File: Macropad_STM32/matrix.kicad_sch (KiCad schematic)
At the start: 85 parts, among them J10 Encoders + LED, J7 Power Connector, J9 Matrix, K1 Kailh Hotswap Socket, K10 Kailh Hotswap Socket, K11 Kailh Hotswap Socket, K12 Kailh Hotswap Socket, K13 Kailh Hotswap Socket, K14 Kailh Hotswap Socket, K15 Kailh Hotswap Socket, K16 Kailh Hotswap Socket, K2 Kailh Hotswap Socket, K3 Kailh Hotswap Socket, K4 Kailh Hotswap Socket, K5 Kailh Hotswap Socket, K6 Kailh Hotswap Socket, K7 Kailh Hotswap Socket, K8 Kailh Hotswap Socket, K9 Kailh Hotswap Socket, SW2 EC11 Encoder, SW3 EC11 Encoder

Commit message: Schematic changes Motherboard nearing completion
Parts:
- removed J10: Encoders + LED, Connector_JST:JST_EH_B7B-EH-A_1x07_P2.50mm_Vertical, symbol Connector_Generic:Conn_01x07
- removed J9: Matrix, Connector_JST:JST_EH_B8B-EH-A_1x08_P2.50mm_Vertical, symbol Connector_Generic:Conn_01x08
- C39, C40, C41, C42: now not fitted
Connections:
- net COL0: no longer K13.1, K14.1, K15.1, K16.1
- net COL1: no longer K10.1, K11.1, K12.1, K9.1
- new net COL2: K10.1, K11.1, K12.1, K9.1
- new net COL3: K13.1, K14.1, K15.1, K16.1
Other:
- company: (none) -> Irfaan
- title: (none) -> STM32 Macropad

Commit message: Revision 1 nearly finished
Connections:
- net ENC1_B is gone; now on net ENC1_A: C39.1, R31.2
- net ENC2_B is gone; now on net ENC2_A: C40.1, R35.2
- net VBUS is gone; now on net +5V: C20.1, C21.1, C29.1, C30.1, C31.1, C32.1, C33.1, C34.1, C35.1, C35.1, C36.1, C36.1, C37.1, C37.1, C38.1, C38.1, D29.1 (VDD), D30.1 (VDD), D31.1 (VDD), D32.1 (VDD), D33.1 (VDD), D34.1 (VDD), D35.1 (VDD), D36.1 (VDD), D37.1 (VDD), D38.1 (VDD), D39.1 (VDD), D40.1 (VDD), D41.1 (VDD), D42.1 (VDD), D43.1 (VDD), D44.1 (VDD), J7.1 (Pin_1)
- net +3.3V renamed +3V3
- net GND renamed GND1
- net GND1: no longer C20.2, C21.2, C29.2, C30.2
- net Key_LED renamed +5V
- new net: C20.2, C21.2, C29.2, C30.2
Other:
- moved on the sheet: C29, C31, C32, C33, C34, C35, C36, C37, C38, C39, C40, C41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

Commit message: Nearly finished Todo: - Fix silkscreen - Final check
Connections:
- net +5V: no longer R27.1
- net ENC1_A: no longer C39.1, R31.2
- net ENC2_A: no longer C40.1, R35.2
- net GND1: now also C20.2, C21.2, C29.2, C30.2
- new net ENC1_B: C39.1, R31.2
- new net ENC2_B: C40.1, R35.2
- new net Key_LED: R27.1
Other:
- moved on the sheet: C39, C40, C41, C42, R27

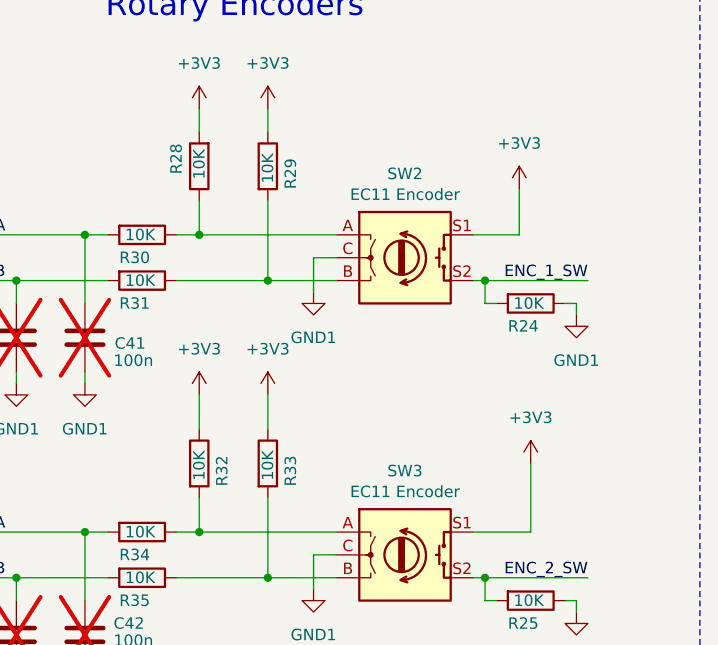
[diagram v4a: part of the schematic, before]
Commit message: Hardware finished and motherboard has been tested. Todo: Test keyboard matrix and write firmware.
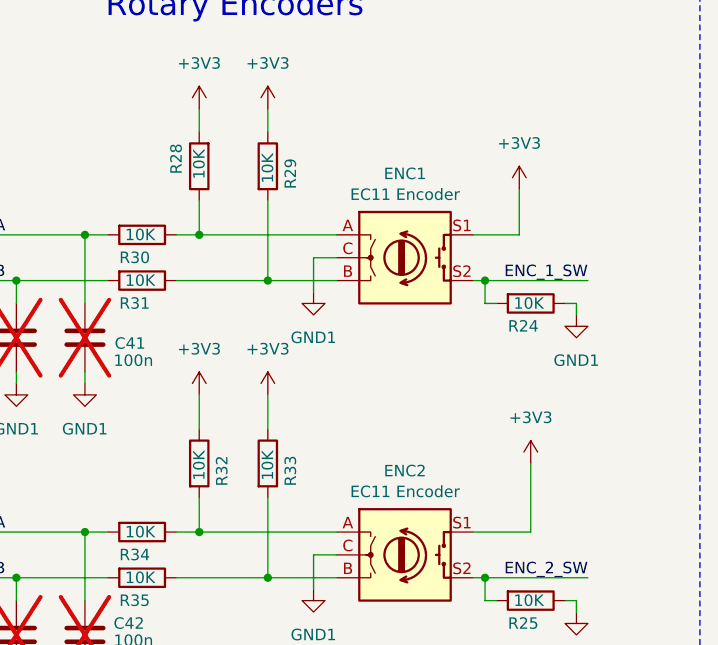
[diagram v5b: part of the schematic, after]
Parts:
- renumbered SW2 to ENC1, SW3 to ENC2
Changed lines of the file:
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@@
         )
         (path "/1bbb8170-4e2d-4119-974a-402fa0f6f9bf/c387cd87-8e18-4230-a191-2ca743b1ddf6"
-          (reference "J12") (unit 1)
+          (reference "POWER2") (unit 1)
         )
       )
@@
   (symbol (lib_id "Hub16-rescue:Rotary_Encoder_Switch-Device") (at 247.65 106.68 0) (unit 1)
     (in_bom yes) (on_board yes) (dnp no)
-    (property "Reference" "SW2" (at 247.65 97.3582 0)
+    (property "Reference" "ENC1" (at 247.65 97.3582 0)
       (effects (font (size 1.27 1.27)))
     )
@@
       (project "Macropad_STM32"
         (path "/1bbb8170-4e2d-4119-974a-402fa0f6f9bf/c387cd87-8e18-4230-a191-2ca743b1ddf6"
-          (reference "SW2") (unit 1)
+          (reference "ENC1") (unit 1)
         )
       )
@@
   (symbol (lib_id "Hub16-rescue:Rotary_Encoder_Switch-Device") (at 247.65 139.7 0) (unit 1)
     (in_bom yes) (on_board yes) (dnp no)
-    (property "Reference" "SW3" (at 247.65 130.3782 0)
+    (property "Reference" "ENC2" (at 247.65 130.3782 0)
       (effects (font (size 1.27 1.27)))
     )
@@
       (project "Macropad_STM32"
         (path "/1bbb8170-4e2d-4119-974a-402fa0f6f9bf/c387cd87-8e18-4230-a191-2ca743b1ddf6"
-          (reference "SW3") (unit 1)
-        )
-      )
+          (reference "ENC2") (unit 1)
+        )
+      )
